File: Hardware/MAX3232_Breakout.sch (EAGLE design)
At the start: 12 parts, among them U1 MAX3232

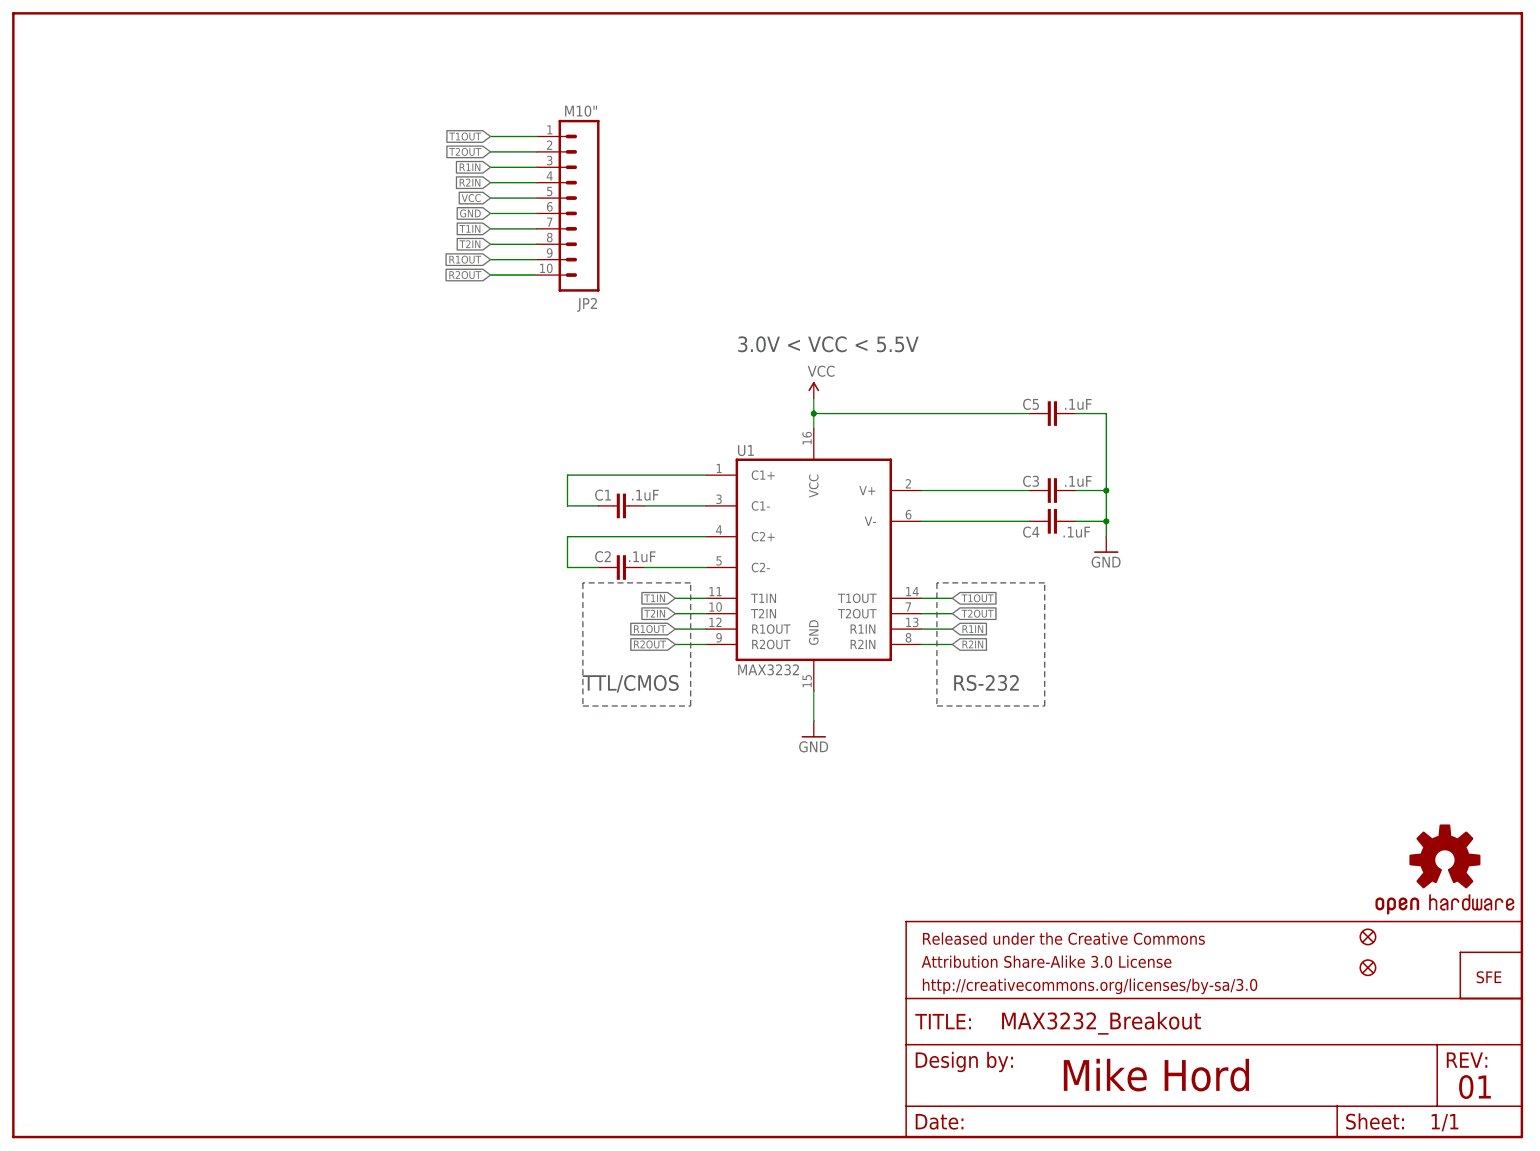
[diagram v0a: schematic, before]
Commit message: Updated to 0603, added attributes.
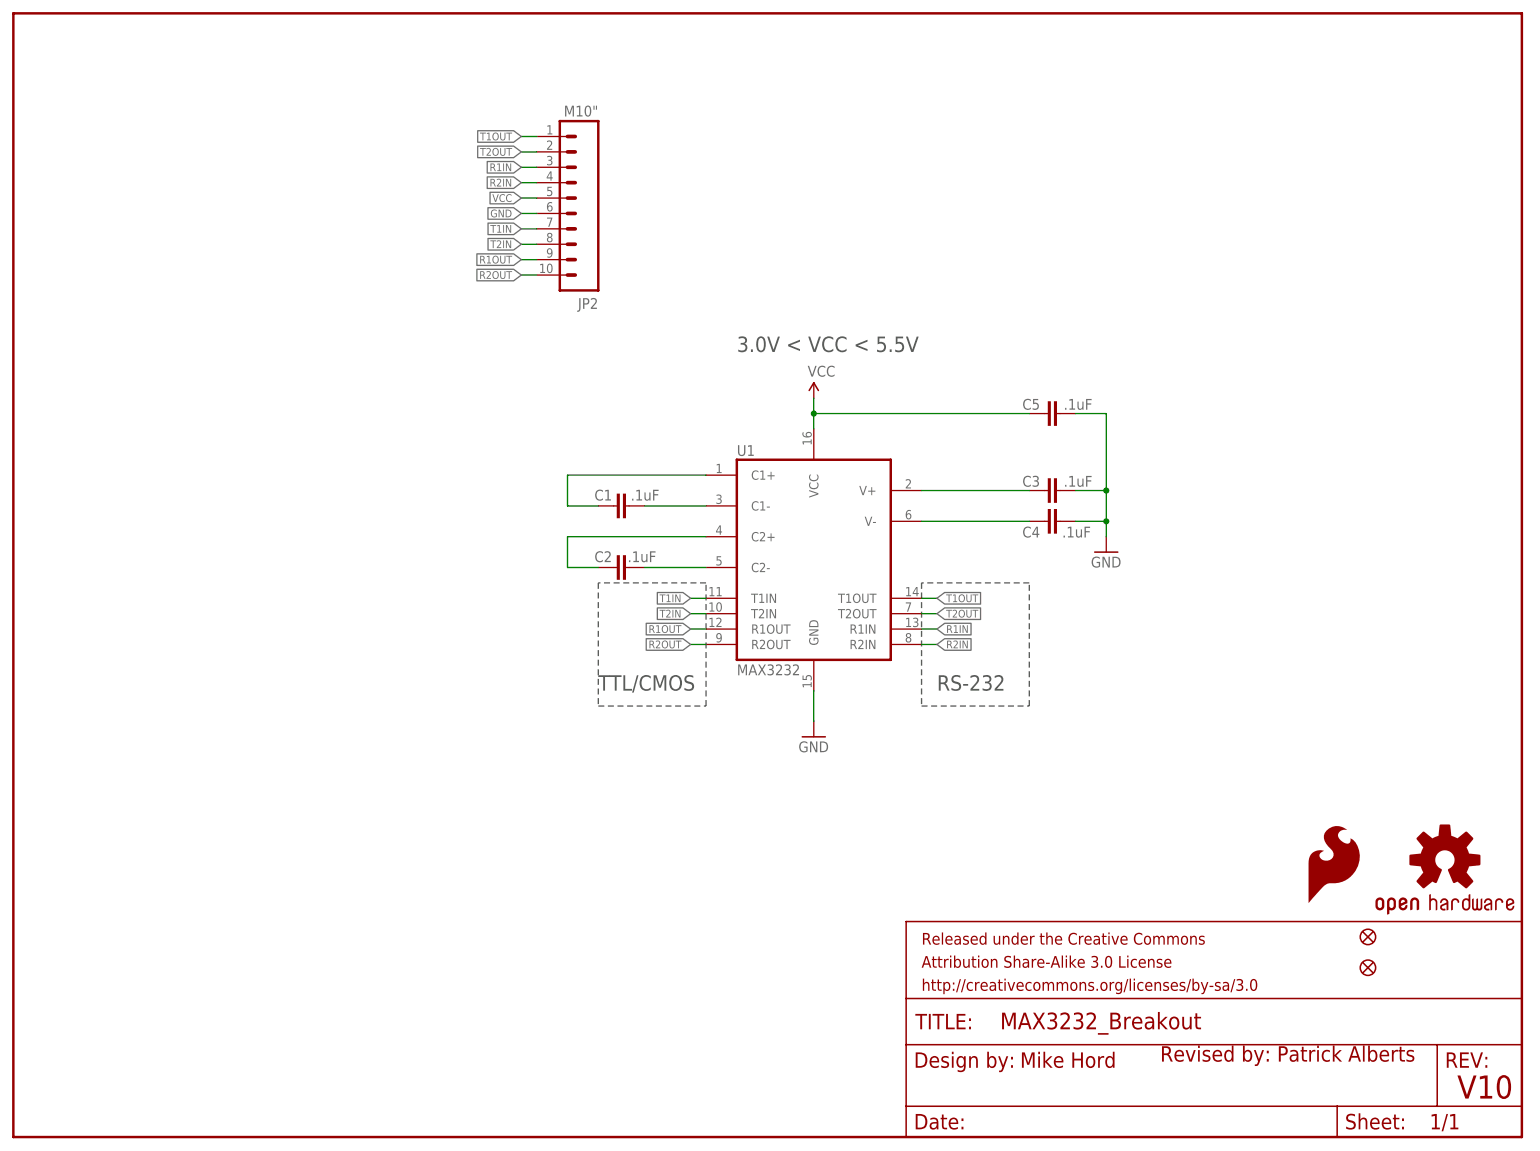
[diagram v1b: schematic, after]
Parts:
- removed JP1: LOGO-SFESK, SparkFun-Aesthetics:LOGO-SFESK
- added LOGO1: SFE_LOGO_FLAME.1_INCH, SparkFun-Aesthetics:SFE_LOGO_FLAME.1_INCH
- C1, C2, C3, C4, C5: device SparkFun-Passives:CAP0402-CAP -> SparkFun-Capacitors:0.1UF-25V(+80/-20%)(0603)
- U$1: value OSHW-LOGOM -> OSHW-LOGOS; device SparkFun-Aesthetics:OSHW-LOGOM -> SparkFun-Aesthetics:OSHW-LOGOS
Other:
- note added: "Revised by: Patrick Alberts"
- note added: "V10"
- note removed: "01"

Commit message: Fixed SCH, re route trace and trestrict
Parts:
- FRAME1: value FRAME-LETTER -> (none)
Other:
- note added: "v11"
- note removed: "V10"
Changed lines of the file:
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@@
 <part name="JP4" library="SparkFun" deviceset="FIDUCIAL" device="UFIDUCIAL"/>
 <part name="LOGO1" library="SparkFun-Aesthetics" deviceset="SFE_LOGO_FLAME" device=".1_INCH"/>
+<part name="P+2" library="SparkFun-Aesthetics" deviceset="VCC" device=""/>
+<part name="GND3" library="SparkFun-Aesthetics" deviceset="GND" device=""/>
 </parts>
 <sheets>
@@
 <text x="119.38" y="129.54" size="2.54" layer="97">3.0V &lt; VCC &lt; 5.5V</text>
 <text x="166.116" y="11.43" size="2.54" layer="94">Mike Hord</text>
-<text x="238.252" y="6.35" size="3.81" layer="94">V10</text>
-<text x="189.23" y="12.446" size="2.54" layer="94" ratio="10">Revised by: Patrick Alberts</text>
+<text x="148.336" y="7.112" size="2.54" layer="94" ratio="10">Revised by: Patrick Alberts</text>
+<text x="238.76" y="7.62" size="2.54" layer="94">v11</text>
 </plain>
 <instances>
@@
 <attribute name="NO_PART" x="0" y="0" size="3.81" layer="96" display="off"/>
 </instance>
-<instance part="FRAME1" gate="G$2" x="147.32" y="0"/>
+<instance part="FRAME1" gate="V" x="147.32" y="0" smashed="yes">
+<attribute name="LAST_DATE_TIME" x="160.02" y="1.27" size="2.54" layer="94" font="vector"/>
+<attribute name="SHEET" x="233.68" y="1.27" size="2.54" layer="94" font="vector"/>
+<attribute name="DRAWING_NAME" x="162.814" y="17.78" size="2.7432" layer="94" font="vector"/>
+</instance>
 <instance part="P+1" gate="1" x="132.08" y="121.92"/>
 <instance part="GND1" gate="1" x="180.34" y="96.52"/>
@@
 <instance part="JP4" gate="G$1" x="223.52" y="27.94"/>
 <instance part="LOGO1" gate="G$1" x="213.36" y="38.1"/>
+<instance part="P+2" gate="1" x="68.58" y="157.48"/>
+<instance part="GND3" gate="1" x="68.58" y="147.32"/>
 </instances>
 <busses>
@@
 </segment>
 <segment>
-<wire x1="86.36" y1="154.94" x2="83.82" y2="154.94" width="0.1524" layer="91"/>
-<label x="83.82" y="154.94" size="1.27" layer="95" rot="MR0" xref="yes"/>
+<wire x1="86.36" y1="154.94" x2="68.58" y2="154.94" width="0.1524" layer="91"/>
+<wire x1="68.58" y1="154.94" x2="68.58" y2="157.48" width="0.1524" layer="91"/>
 <pinref part="JP2" gate="G$1" pin="5"/>
+<pinref part="P+2" gate="1" pin="VCC"/>
 </segment>
 </net>
@@
 </segment>
 <segment>
-<wire x1="86.36" y1="152.4" x2="83.82" y2="152.4" width="0.1524" layer="91"/>
-<label x="83.82" y="152.4" size="1.27" layer="95" rot="MR0" xref="yes"/>
+<wire x1="86.36" y1="152.4" x2="68.58" y2="152.4" width="0.1524" layer="91"/>
+<wire x1="68.58" y1="152.4" x2="68.58" y2="149.86" width="0.1524" layer="91"/>
 <pinref part="JP2" gate="G$1" pin="6"/>
+<pinref part="GND3" gate="1" pin="GND"/>
 </segment>
 </net>
